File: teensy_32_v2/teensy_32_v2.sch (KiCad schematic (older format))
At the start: 2 parts, among them P1 RPI_GPIO

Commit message: move forward on new hat
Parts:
- P1: value RPI_GPIO -> S9200-ND; footprint (none) -> teensy:RPI_BOTTOM_NOLABELS
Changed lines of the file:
@@
 P 9450 3250
 F 0 "P1" H 9500 4250 50  0000 C CNN
-F 1 "RPI_GPIO" H 9500 2150 50  0000 C CNN
-F 2 "" H 9450 3250 50  0001 C CNN
+F 1 "S9200-ND" H 9500 2150 50  0000 C CNN
+F 2 "teensy:RPI_BOTTOM_NOLABELS" H 9450 3250 50  0001 C CNN
 F 3 "" H 9450 3250 50  0001 C CNN
 	1    9450 3250

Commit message: more hat
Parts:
- U1: renamed from U?; footprint (none) -> teensy:TEENSY_3
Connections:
- net labels added: +3.3VP, CRX, CTX, IN_AUX, IN_STEER, IN_THROTTLE, OUT_AUX, OUT_STEER, OUT_THROTTLE, T_A8, T_A9, T_RX1, T_RX2, T_TX1, T_TX2
- wire segments 38 -> 74
- no-connect marks 2 -> 29

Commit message: another attempt at Hat layout -- pre routing
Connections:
- wire segments 74 -> 78
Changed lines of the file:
@@
 F14 "T_RX2" I L 5300 2550 60
 F15 "T_TX2" I L 5300 2650 60
+F16 "T_SDA" I R 6450 2050 60
+F17 "T_SCL" I R 6450 2200 60
+F18 "T_RX3" I R 6450 2400 60
+F19 "T_TX3" I R 6450 2550 60
 $EndSheet
 $Comp
@@
 	1    0    0    -1
 $EndComp
+Text Label 6850 2550 2    60   ~ 0
+T_TX3
+Text Label 6850 2400 2    60   ~ 0
+T_RX3
+Text Label 6850 2200 2    60   ~ 0
+T_SCL
+Text Label 6850 2050 2    60   ~ 0
+T_SDA
+Wire Wire Line
+	6950 2550 6450 2550
+Wire Wire Line
+	6950 2400 6450 2400
+Wire Wire Line
+	6950 2200 6450 2200
+Wire Wire Line
+	6950 2050 6450 2050
 $EndSCHEMATC

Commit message: Macrofab proto order of teensy hat v2b
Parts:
- U1: value TEENSY_3 -> ED28DT
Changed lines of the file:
@@
 P 2000 4650
 F 0 "U1" H 2200 3450 60  0000 C CNN
-F 1 "TEENSY_3" H 2200 6150 60  0000 C CNN
+F 1 "ED28DT" H 2200 6150 60  0000 C CNN
 F 2 "teensy:TEENSY_3" H 2000 4650 60  0001 C CNN
 F 3 "" H 2000 4650 60  0000 C CNN

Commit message: update teensy hat schematic
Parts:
- added D6: MF-LED-0603-RED, MF_LEDs:MF_LEDs-LED0603, symbol LED_SINGLE-0603-GREEN
- added R17: MF-RES-0603-2K, MF_Passives:MF_Passives-R0603, symbol RESISTOR_0805
- U1: value ED28DT -> TEENSY
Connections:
- net labels added: MSG_LED
- wire segments 78 -> 82
- no-connect marks 29 -> 28
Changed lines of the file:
@@
 P 2000 4650
 F 0 "U1" H 2200 3450 60  0000 C CNN
-F 1 "ED28DT" H 2200 6150 60  0000 C CNN
+F 1 "TEENSY" H 2200 6150 60  0000 C CNN
 F 2 "teensy:TEENSY_3" H 2000 4650 60  0001 C CNN
 F 3 "" H 2000 4650 60  0000 C CNN
@@
 Text Label 4700 2650 0    60   ~ 0
 T_TX2
-NoConn ~ 3000 5450
 NoConn ~ 3000 5050
 NoConn ~ 3000 4850
@@
 Wire Wire Line
 	6950 2050 6450 2050
+Wire Wire Line
+	3000 5450 3850 5450
+Wire Wire Line
+	3850 5450 3850 5850
+$Comp
+L RESISTOR_0805 R?
+U 1 1 5A472546
+P 3850 6050
+AR Path="/59ED6513/5A472546" Ref="R?"  Part="1"
+AR Path="/5A472546" Ref="R17"  Part="1"
+F 0 "R17" V 3750 6000 45  0000 L BNN
+F 1 "MF-RES-0603-2K" V 4000 5650 45  0000 L BNN
+F 2 "MF_Passives:MF_Passives-R0603" H 4100 5960 20  0001 C CNN
+F 3 "" H 3850 6050 60  0001 C CNN
+	1    3850 6050
+	1    0    0    1
+$EndComp
+$Comp
+L LED_SINGLE-0603-GREEN D?
+U 1 1 5A47254D
+P 3850 6500
+AR Path="/59ED6513/5A47254D" Ref="D?"  Part="1"
+AR Path="/5A47254D" Ref="D6"  Part="1"
+F 0 "D6" H 3800 6350 45  0000 L BNN
+F 1 "MF-LED-0603-RED" H 3450 6250 45  0000 L BNN
+F 2 "MF_LEDs:MF_LEDs-LED0603" H 3890 6270 20  0001 C CNN
+F 3 "" H 3850 6500 60  0001 C CNN
+	1    3850 6500
+	0    1    1    0
+$EndComp
+$Comp
+L GND #PWR010
+U 1 1 5A472554
+P 3850 6700
+F 0 "#PWR010" H 3850 6450 50  0001 C CNN
+F 1 "GND" H 3850 6550 50  0000 C CNN
+F 2 "" H 3850 6700 50  0001 C CNN
+F 3 "" H 3850 6700 50  0001 C CNN
+	1    3850 6700
+	1    0    0    -1
+$EndComp
+Wire Wire Line
+	3850 6250 3850 6400
+Wire Wire Line
+	3850 6600 3850 6700
+Text Label 3150 5450 0    60   ~ 0
+MSG_LED
 $EndSCHEMATC

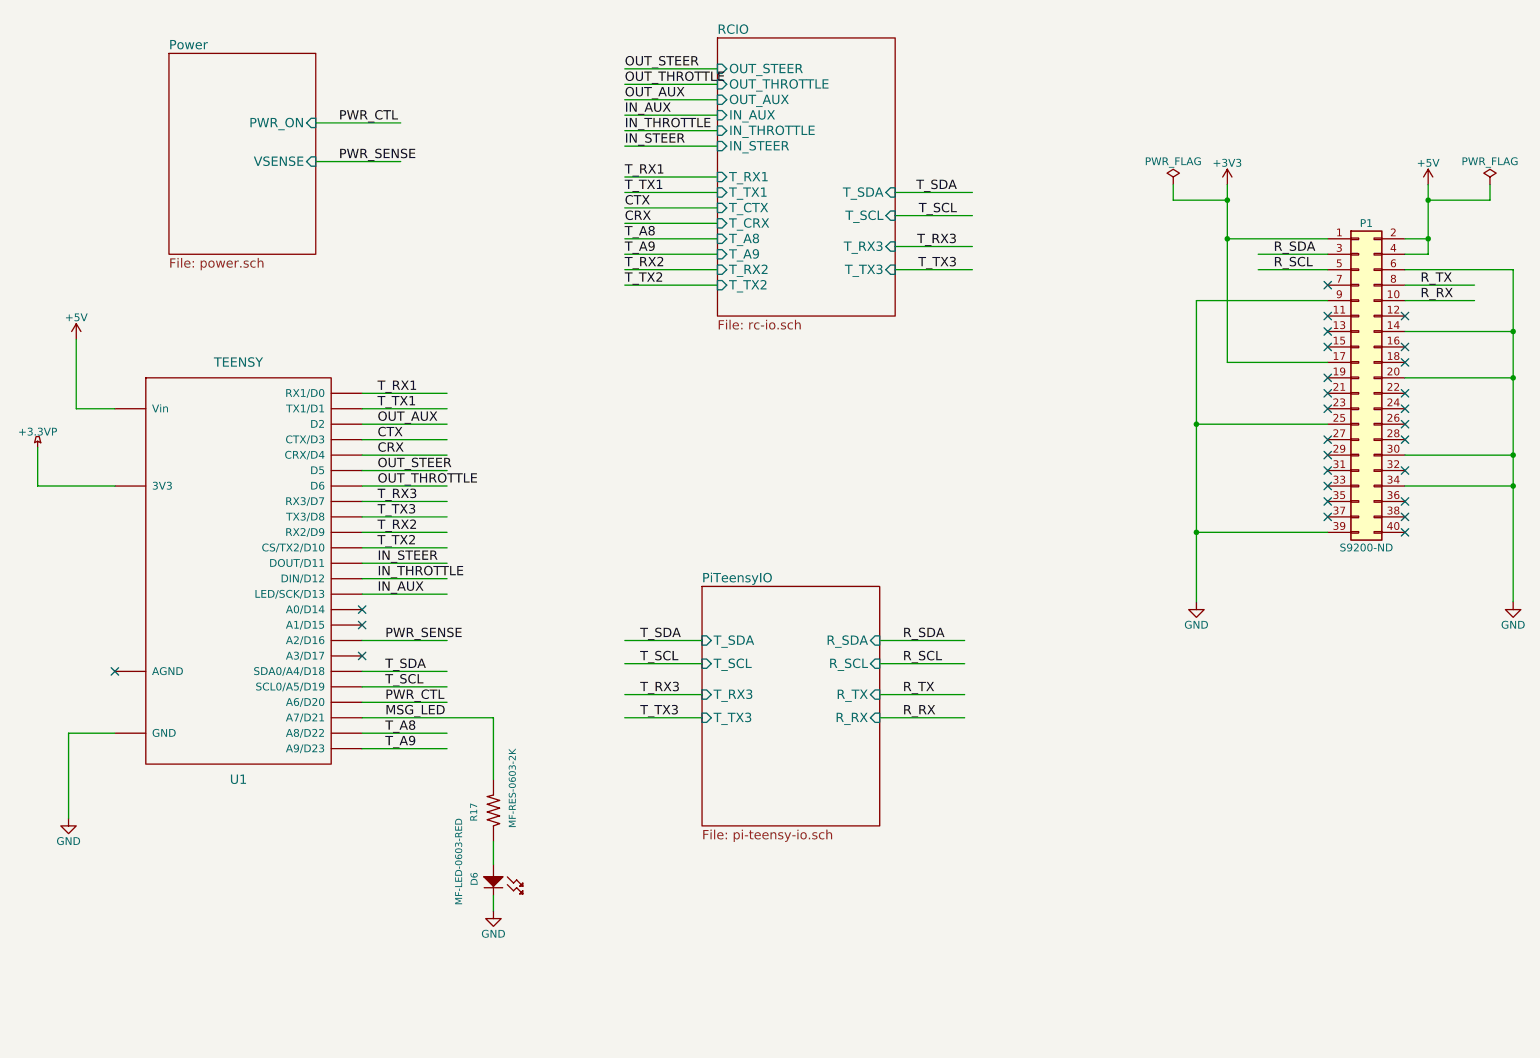
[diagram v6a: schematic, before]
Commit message: Updates to hat for next manufacturing run (pre order)
remove unused directories

move over teensy3.lib library that was needed
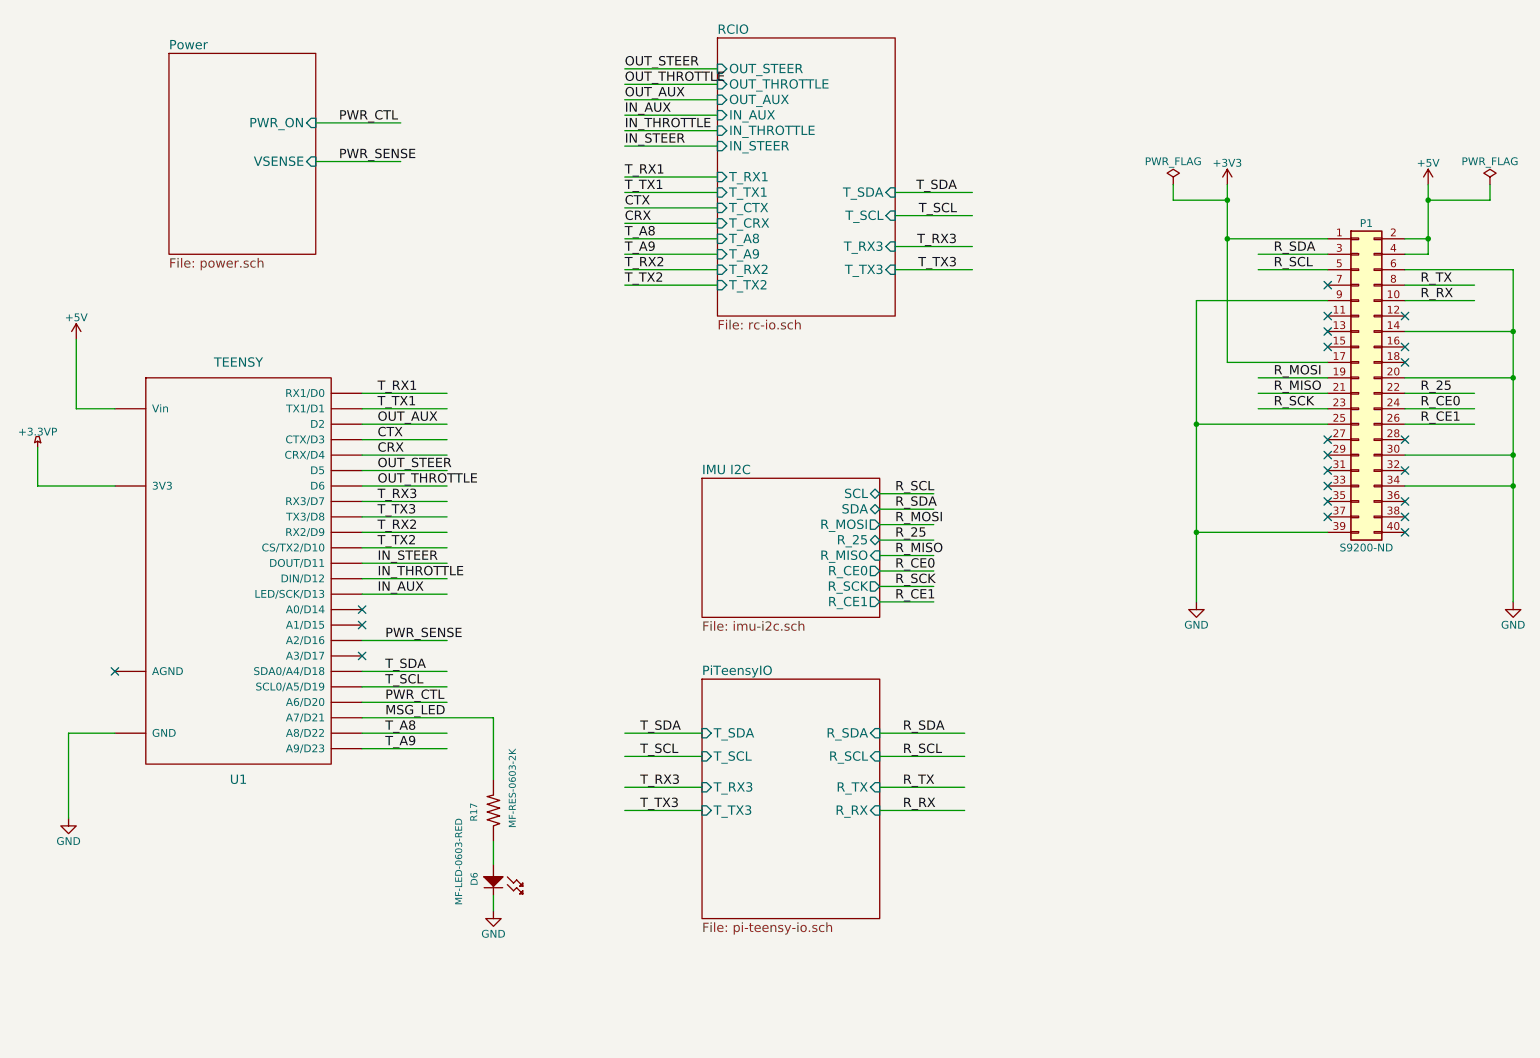
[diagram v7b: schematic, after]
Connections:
- net labels added: R_25, R_CE0, R_CE1, R_MISO, R_MOSI, R_SCK
- wire segments 82 -> 96
- no-connect marks 28 -> 22
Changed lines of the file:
@@
 $Descr A4 11693 8268
 encoding utf-8
-Sheet 1 4
+Sheet 1 5
 Title ""
 Date ""
@@
 $EndSheet
 $Sheet
-S 5200 4600 1150 1550
+S 5200 5200 1150 1550
 U 59ED67C6
 F0 "PiTeensyIO" 60
 F1 "pi-teensy-io.sch" 60
-F2 "R_SDA" I R 6350 4950 60
-F3 "R_SCL" I R 6350 5100 60
-F4 "R_TX" I R 6350 5300 60
-F5 "R_RX" I R 6350 5450 60
-F6 "T_SDA" I L 5200 4950 60
-F7 "T_SCL" I L 5200 5100 60
-F8 "T_RX3" I L 5200 5300 60
-F9 "T_TX3" I L 5200 5450 60
+F2 "R_SDA" I R 6350 5550 60
+F3 "R_SCL" I R 6350 5700 60
+F4 "R_TX" I R 6350 5900 60
+F5 "R_RX" I R 6350 6050 60
+F6 "T_SDA" I L 5200 5550 60
+F7 "T_SCL" I L 5200 5700 60
+F8 "T_RX3" I L 5200 5900 60
+F9 "T_TX3" I L 5200 6050 60
 $EndSheet
 $Sheet
@@
 	1    0    0    -1
 $EndComp
-Text Label 6500 4950 0    60   ~ 0
+Text Label 6500 5550 0    60   ~ 0
 R_SDA
-Text Label 6500 5100 0    60   ~ 0
+Text Label 6500 5700 0    60   ~ 0
 R_SCL
-Text Label 6500 5300 0    60   ~ 0
+Text Label 6500 5900 0    60   ~ 0
 R_TX
-Text Label 6500 5450 0    60   ~ 0
+Text Label 6500 6050 0    60   ~ 0
 R_RX
-Text Label 4800 5450 0    60   ~ 0
+Text Label 4800 6050 0    60   ~ 0
 T_TX3
-Text Label 4800 5300 0    60   ~ 0
+Text Label 4800 5900 0    60   ~ 0
 T_RX3
-Text Label 4800 5100 0    60   ~ 0
+Text Label 4800 5700 0    60   ~ 0
 T_SCL
-Text Label 4800 4950 0    60   ~ 0
+Text Label 4800 5550 0    60   ~ 0
 T_SDA
 Text Label 9850 2650 0    60   ~ 0
@@
 R_SCL
 Wire Wire Line
-	9750 2350 9900 2350
+	9900 2350 9750 2350
 Wire Wire Line
 	9900 2000 9900 2450
@@
 	1150 3450 1400 3450
 Wire Wire Line
-	9250 2350 8600 2350
+	8600 2350 9250 2350
 Wire Wire Line
 	8600 2000 8600 3150
@@
 	10450 2550 10450 4700
 Wire Wire Line
-	6350 4950 6900 4950
-Wire Wire Line
-	6350 5100 6900 5100
-Wire Wire Line
-	6350 5300 6900 5300
-Wire Wire Line
-	6350 5450 6900 5450
-Wire Wire Line
-	4700 5450 5200 5450
-Wire Wire Line
-	4700 5300 5200 5300
-Wire Wire Line
-	4700 5100 5200 5100
-Wire Wire Line
-	4700 4950 5200 4950
+	6350 5550 6900 5550
+Wire Wire Line
+	6350 5700 6900 5700
+Wire Wire Line
+	6350 5900 6900 5900
+Wire Wire Line
+	6350 6050 6900 6050
+Wire Wire Line
+	4700 6050 5200 6050
+Wire Wire Line
+	4700 5900 5200 5900
+Wire Wire Line
+	4700 5700 5200 5700
+Wire Wire Line
+	4700 5550 5200 5550
 Wire Wire Line
 	9750 2650 10200 2650
@@
 NoConn ~ 9250 2950
 NoConn ~ 9250 3050
-NoConn ~ 9250 3250
-NoConn ~ 9250 3350
-NoConn ~ 9250 3450
 NoConn ~ 9250 3650
 NoConn ~ 9250 3750
@@
 NoConn ~ 9750 3850
 NoConn ~ 9750 3650
-NoConn ~ 9750 3550
-NoConn ~ 9750 3450
-NoConn ~ 9750 3350
 NoConn ~ 9750 3150
 NoConn ~ 9750 3050
@@
 Text Label 3150 5450 0    60   ~ 0
 MSG_LED
+$Sheet
+S 5200 3900 1150 900
+U 5A8B3766
+F0 "IMU I2C" 60
+F1 "imu-i2c.sch" 60
+F2 "SCL" B R 6350 4000 60
+F3 "SDA" B R 6350 4100 60
+F4 "R_MOSI" O R 6350 4200 60
+F5 "R_25" B R 6350 4300 60
+F6 "R_MISO" I R 6350 4400 60
+F7 "R_CE0" O R 6350 4500 60
+F8 "R_SCK" O R 6350 4600 60
+F9 "R_CE1" O R 6350 4700 60
+$EndSheet
+Wire Wire Line
+	6350 4000 6700 4000
+Wire Wire Line
+	6350 4100 6700 4100
+Text Label 6450 4000 0    60   ~ 0
+R_SCL
+Text Label 6450 4100 0    60   ~ 0
+R_SDA
+Wire Wire Line
+	9250 3250 8800 3250
+Wire Wire Line
+	9250 3350 8800 3350
+Wire Wire Line
+	9250 3450 8800 3450
+Wire Wire Line
+	9750 3350 10200 3350
+Wire Wire Line
+	9750 3450 10200 3450
+Wire Wire Line
+	9750 3550 10200 3550
+Text Label 8900 3250 0    60   ~ 0
+R_MOSI
+Text Label 8900 3350 0    60   ~ 0
+R_MISO
+Text Label 8900 3450 0    60   ~ 0
+R_SCK
+Text Label 9850 3350 0    60   ~ 0
+R_25
+Text Label 9850 3450 0    60   ~ 0
+R_CE0
+Text Label 9850 3550 0    60   ~ 0
+R_CE1
+Wire Wire Line
+	6350 4200 6700 4200
+Wire Wire Line
+	6350 4300 6700 4300
+Wire Wire Line
+	6350 4400 6700 4400
+Wire Wire Line
+	6350 4500 6700 4500
+Wire Wire Line
+	6350 4600 6700 4600
+Wire Wire Line
+	6350 4700 6700 4700
+Text Label 6450 4200 0    60   ~ 0
+R_MOSI
+Text Label 6450 4300 0    60   ~ 0
+R_25
+Text Label 6450 4400 0    60   ~ 0
+R_MISO
+Text Label 6450 4500 0    60   ~ 0
+R_CE0
+Text Label 6450 4600 0    60   ~ 0
+R_SCK
+Text Label 6450 4700 0    60   ~ 0
+R_CE1
 $EndSCHEMATC
